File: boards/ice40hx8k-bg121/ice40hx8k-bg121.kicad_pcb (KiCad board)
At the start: 4 copper layers, 22.9 x 50.5 mm, 59 parts, among them J1 BANK 0, J2 BANK 1, J4 BANK 2, J5 BANK 3, U1 AP7361C_TO252_DPAK, U2 AP7361C_TO252_DPAK, U3 iCE40HX8K-BG121(121-Ball_caBG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, U4 ASDMB-xxxMHz

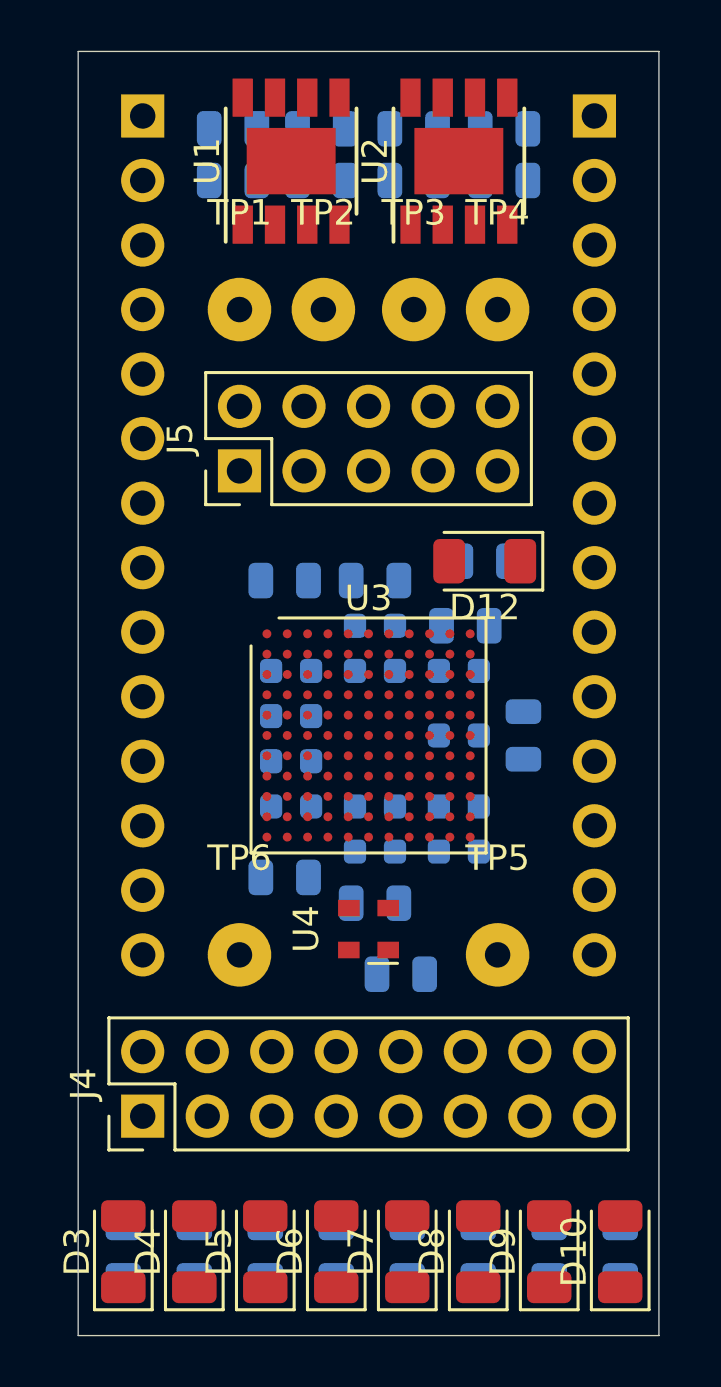
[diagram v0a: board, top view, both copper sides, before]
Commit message: Started putting down traces.
Still need to do C and differential pairs D.
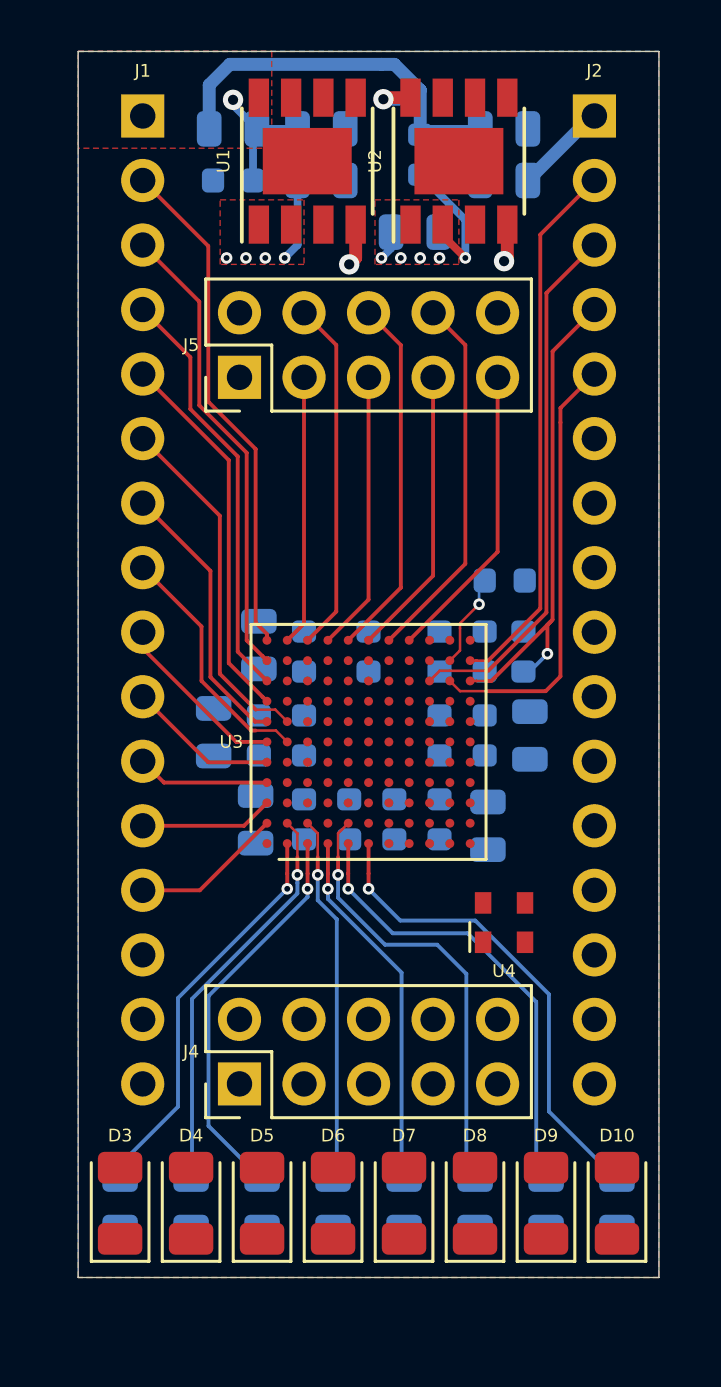
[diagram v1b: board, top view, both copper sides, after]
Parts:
- removed D12: CDONE, LED_SMD:LED_1206_3216Metric
- removed R15: 4k7, Diode_SMD:D_0805_2012Metric
- removed TP1: 3V3_EN, Connector_Wire:SolderWirePad_1x01_Drill1mm
- removed TP2: 1V2_IN, Connector_Wire:SolderWirePad_1x01_Drill1mm
- removed TP3: 1V2_OUT, Connector_Wire:SolderWirePad_1x01_Drill1mm
- removed TP4: 1V2_EN, Connector_Wire:SolderWirePad_1x01_Drill1mm
- removed TP5: OSC_STBY, Connector_Wire:SolderWirePad_1x01_Drill1mm
- removed TP6: FPGA_CLK, Connector_Wire:SolderWirePad_1x01_Drill1mm
- J1, J2: footprint Connector_PinHeader_2.54mm:PinHeader_1x14_P2.54mm_Vertical -> Connector_PinHeader_2.54mm:PinHeader_1x16_P2.54mm_Vertical
- J4: footprint Connector_PinHeader_2.54mm:PinHeader_2x08_P2.54mm_Vertical -> Connector_PinHeader_2.54mm:PinHeader_2x05_P2.54mm_Vertical
- R1, R13, R2: footprint Diode_SMD:D_0805_2012Metric -> Resistor_SMD:R_0603_1608Metric
- R10, R11, R12, R3, R4, R5, R6, R7, R8, R9: footprint Diode_SMD:D_0805_2012Metric -> Resistor_SMD:R_0805_2012Metric
- R14: value 220R -> 4k7; footprint Diode_SMD:D_0805_2012Metric -> Resistor_SMD:R_0603_1608Metric
- U1, U2: value AP7361C_TO252_DPAK -> AP7361C_SO-8EP
- moved R12 9.47 mm to (27.3, 45.5), turned to 90 degrees
- moved C9 8.99 mm to (38.1, 42.2), turned to 270 degrees
- moved C14 8.72 mm to (25.7, 42.0), turned to 90 degrees
- moved R11 8.25 mm to (36.4, 45.7), turned to 90 degrees
- moved D11 8.16 mm to (27.4, 38.6), turned to 90 degrees
- moved C17 7.94 mm to (36.3, 38.9), turned to 270 degrees
- moved C15 6.29 mm to (27.4, 42.2), turned to 90 degrees
- moved C10 6.29 mm to (36.3, 42.2), turned to 270 degrees
- moved C5 6.14 mm to (29.2, 38.9), turned to 270 degrees
- moved C7 6.14 mm to (34.5, 38.9), turned to 270 degrees
- moved R13 6.14 mm to (37.1, 36.1), turned to 0 degrees
- moved C6 5.86 mm to (29.2, 45.5), turned to 90 degrees
- moved C8 5.86 mm to (34.5, 45.5), turned to 90 degrees
- moved U4 5.34 mm to (37.1, 49.5), turned to 0 degrees
- moved C12 4.85 mm to (31.8, 38.9), turned to 270 degrees
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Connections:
- J1 pad 12: VCCIO_A -> IO_A10
- J1 pad 13: +3V3 -> IO_A11
- J1 pad 14: GND -> VCCIO_A
- J2 pad 10: IO_B08 -> IO_C03
- J2 pad 11: IO_B09 -> IO_C02
- J2 pad 12: VCCIO_B -> IO_C01
- J2 pad 13: +3V3 -> IO_C00
- J2 pad 14: GND -> VCCIO_B
- J2 pad 2: IO_B00 -> PROG_SCK
- J2 pad 3: IO_B01 -> PROG_SDI
- J2 pad 4: IO_B02 -> PROG_CRESET_B
- J2 pad 5: IO_B03 -> PROG_SDO
- J2 pad 6: IO_B04 -> IO_C07
- J2 pad 7: IO_B05 -> IO_C06
- J2 pad 8: IO_B06 -> IO_C05
- J2 pad 9: IO_B07 -> IO_C04
- J4 pad 1: IO_C00 -> +3V3
- J4 pad 10: PROG_CRESET_B -> GND
- J4 pad 2: +3V3 -> VCCIO_D
- J4 pad 3: IO_C01 -> IO_D00+
- J4 pad 4: VCCIO_C -> IO_D03
- J4 pad 5: IO_C02 -> IO_D00-
- J4 pad 6: PROG_SDO -> IO_D02-
- J4 pad 7: IO_C03 -> IO_D01+
- J4 pad 8: PROG_SDI -> IO_D02+
- J4 pad 9: IO_C04 -> IO_D01-
- J5 pad 1: IO_D00+ -> VCCIO_B
- J5 pad 3: IO_D00- -> IO_B00
- J5 pad 4: VCCIO_D -> IO_B06
- J5 pad 5: IO_D01+ -> IO_B01
- J5 pad 6: IO_D01- -> IO_B05
- J5 pad 7: IO_D02+ -> IO_B02
- J5 pad 8: IO_D03 -> IO_B04
- J5 pad 9: IO_D02- -> IO_B03
- R10 pad 1: IO_C00 -> IO_L0
- R14 pad 1: /ICE40HX8K/CDONE -> VCCIO_C
- R14 pad 2: Net-(D12-Pad1) -> PROG_CRESET_B
- R3 pad 1: IO_C07 -> IO_L7
- R4 pad 1: IO_C06 -> IO_L6
- R5 pad 1: IO_C05 -> IO_L5
- R6 pad 1: IO_C04 -> IO_L4
- R7 pad 1: IO_C03 -> IO_L3
- R8 pad 1: IO_C02 -> IO_L2
- R9 pad 1: IO_C01 -> IO_L1
- U1 pad 9: (no net) -> GND
- U2 pad 9: (no net) -> GND
- U3 pad A1: IO_A02 -> Net-(U3-PadA1)
- U3 pad A10: IO_A09 -> IO_A01
- U3 pad A11: IO_A08 -> IO_A00
- U3 pad A2: IO_A04 -> IO_A11
- U3 pad A3: IO_A03 -> IO_A10
- U3 pad A4: Net-(U3-PadA4) -> IO_A09
- U3 pad A5: Net-(U3-PadA5) -> IO_A08
- U3 pad A6: Net-(U3-PadA6) -> IO_A07
- U3 pad A7: Net-(U3-PadA7) -> IO_A05
- U3 pad A8: Net-(U3-PadA8) -> IO_A03
- U3 pad A9: Net-(U3-PadA9) -> IO_A02
- U3 pad B1: IO_D00+ -> IO_L7
- U3 pad B11: IO_B02 -> IO_B00
- U3 pad B2: IO_D00- -> IO_L6
- U3 pad B3: IO_A05 -> Net-(U3-PadB3)
- U3 pad B4: IO_A06 -> Net-(U3-PadB4)
- U3 pad B6: IO_A00 -> IO_A06
- U3 pad B7: IO_A01 -> IO_A04
- U3 pad C1: IO_D02- -> IO_L5
- U3 pad C11: IO_B03 -> IO_B06
- U3 pad C2: IO_D02+ -> IO_L4
- U3 pad C3: IO_D01- -> Net-(U3-PadC3)
- U3 pad C4: IO_D01+ -> Net-(U3-PadC4)
- U3 pad D1: IO_D03- -> IO_L3
- U3 pad D10: IO_B04 -> Net-(U3-PadD10)
- U3 pad D11: IO_B05 -> IO_B01
- U3 pad D5: IO_A07 -> Net-(U3-PadD5)
- U3 pad D9: IO_B07 -> Net-(U3-PadD9)
- U3 pad E1: IO_D03+ -> IO_L1
- U3 pad E10: IO_B00 -> Net-(U3-PadE10)
- U3 pad E11: IO_B06 -> IO_B05
- U3 pad E2: Net-(U3-PadE2) -> IO_L2
- U3 pad F1: Net-(U3-PadF1) -> IO_L0
- U3 pad F11: IO_B01 -> IO_B02
- U3 pad F3: IO_D04 -> IO_D03
- U3 pad G1: Net-(U3-PadG1) -> IO_D00-
- U3 pad G11: Net-(U3-PadG11) -> IO_B04
- U3 pad G2: Net-(U3-PadG2) -> IO_D00+
- U3 pad H1: Net-(U3-PadH1) -> IO_D02+
- U3 pad H11: Net-(U3-PadH11) -> IO_B03
- U3 pad H2: Net-(U3-PadH2) -> IO_D02-
- U3 pad J1: Net-(U3-PadJ1) -> IO_D01+
- U3 pad J11: IO_B08 -> Net-(U3-PadJ11)
- U3 pad J3: IO_C02 -> Net-(U3-PadJ3)
- U3 pad J4: IO_C05 -> Net-(U3-PadJ4)
- U3 pad K1: Net-(U3-PadK1) -> IO_D01-
- U3 pad K11: IO_B09 -> Net-(U3-PadK11)
- U3 pad K3: IO_C04 -> IO_C03
- U3 pad K4: Net-(U3-PadK4) -> IO_C05
- U3 pad K5: Net-(U3-PadK5) -> IO_C06
- U3 pad K6: IO_C00 -> IO_C07
- U3 pad K8: /ICE40HX8K/CDONE -> Net-(U3-PadK8)
- U3 pad L1: IO_C01 -> IO_C00
- U3 pad L2: IO_C03 -> IO_C01
- U3 pad L3: IO_C06 -> IO_C02
- U3 pad L4: IO_C07 -> IO_C04
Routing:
- net PROG_SCK: track 0.00 -> 21.3 mm
- net PROG_SDI: track 0.00 -> 21.0 mm
- net IO_A00: track 0.00 -> 20.1 mm
- net Net-(C3-Pad1): track 0.00 -> 19.7 mm, vias 0 -> 1
- net PROG_CRESET_B: track 0.00 -> 19.7 mm, vias 0 -> 1
- net IO_L0: track 0.00 -> 19.0 mm, vias 0 -> 1
- net IO_A01: track 0.00 -> 18.4 mm
- net IO_L1: track 0.00 -> 18.2 mm, vias 0 -> 1
- net IO_L2: track 0.00 -> 17.6 mm, vias 0 -> 1
- net PROG_SDO: track 0.00 -> 17.2 mm
- net IO_A02: track 0.00 -> 16.6 mm
- net IO_L7: track 0.00 -> 15.9 mm, vias 0 -> 1
- net IO_L6: track 0.00 -> 15.9 mm, vias 0 -> 1
- net IO_L5: track 0.00 -> 15.7 mm, vias 0 -> 1
- net IO_A03: track 0.00 -> 14.9 mm
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- added copper zone on F.Cu, net +1V2
- added copper zone on F.Cu, net +3V3
- added copper zone on In1.Cu, net +3V3
- added copper zone on F.Cu, net +5V
- added copper zone on B.Cu, net GND
- added copper zone on F.Cu, net GND
- added copper zone on In2.Cu, net GND
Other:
- board size 22.9 x 50.5 mm -> 22.9 x 48.3 mm
- net class Default: clearance 0.2 -> 0.0889
- rule trace_clearance: 0.2 -> 0.0889
- rule trace_min: 0.2 -> 0.0889
- rule via_min_drill: 0.3 -> 0.2
- rule via_min_size: 0.4 -> 0.45

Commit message: Starting ISL83488 breakout
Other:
- board text added: "Oh yeah, this thing can be like 1.5-2x long."
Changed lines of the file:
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@@
   (general
     (thickness 1.6)
-    (drawings 5)
+    (drawings 6)
     (tracks 222)
     (zones 0)
@@
     (39 F.Mask user)
     (40 Dwgs.User user hide)
-    (41 Cmts.User user hide)
+    (41 Cmts.User user)
     (42 Eco1.User user hide)
     (43 Eco2.User user hide)
@@
   )
   (setup
-    (last_trace_width 0.508)
+    (last_trace_width 0.25)
     (user_trace_width 0.1016)
     (user_trace_width 0.1524)
@@
     )
   )
+  (gr_text "Oh yeah, this thing can be like 1.5-2x long." (at 73.7616 35.306) (layer Cmts.User)
+    (effects (font (size 1.5 1.5) (thickness 0.3)))
+  )
   (dimension 17.78 (width 0.15) (layer Cmts.User)
     (gr_text "0.7000 in" (at 31.75 14.194) (layer Cmts.User)
@@
   (segment (start 37.211 22.0555) (end 37.211 23.368) (width 0.508) (layer F.Cu) (net 1))
   (segment (start 37.211 23.368) (end 37.084 23.495) (width 0.508) (layer F.Cu) (net 1))
-  (via (at 32.3342 17.1196) (size 0.8) (drill 0.4) (layers F.Cu B.Cu) (net 6))
   (via (at 26.162 23.368) (size 0.4572) (drill 0.2286) (layers F.Cu B.Cu) (net 2))
   (via (at 27.686 23.368) (size 0.4572) (drill 0.2286) (layers F.Cu B.Cu) (net 2))
@@
   (segment (start 27.3535 18.288) (end 26.416 17.3505) (width 0.3048) (layer B.Cu) (net 3))
   (via (at 26.416 17.145) (size 0.8) (drill 0.4) (layers F.Cu B.Cu) (net 3))
+  (via (at 32.3342 17.1196) (size 0.8) (drill 0.4) (layers F.Cu B.Cu) (net 6))
   (segment (start 36.1465 20.32) (end 36.1465 18.288) (width 0.3048) (layer B.Cu) (net 6))
   (segment (start 34.0105 18.288) (end 33.782 18.5165) (width 0.3048) (layer B.Cu) (net 6))

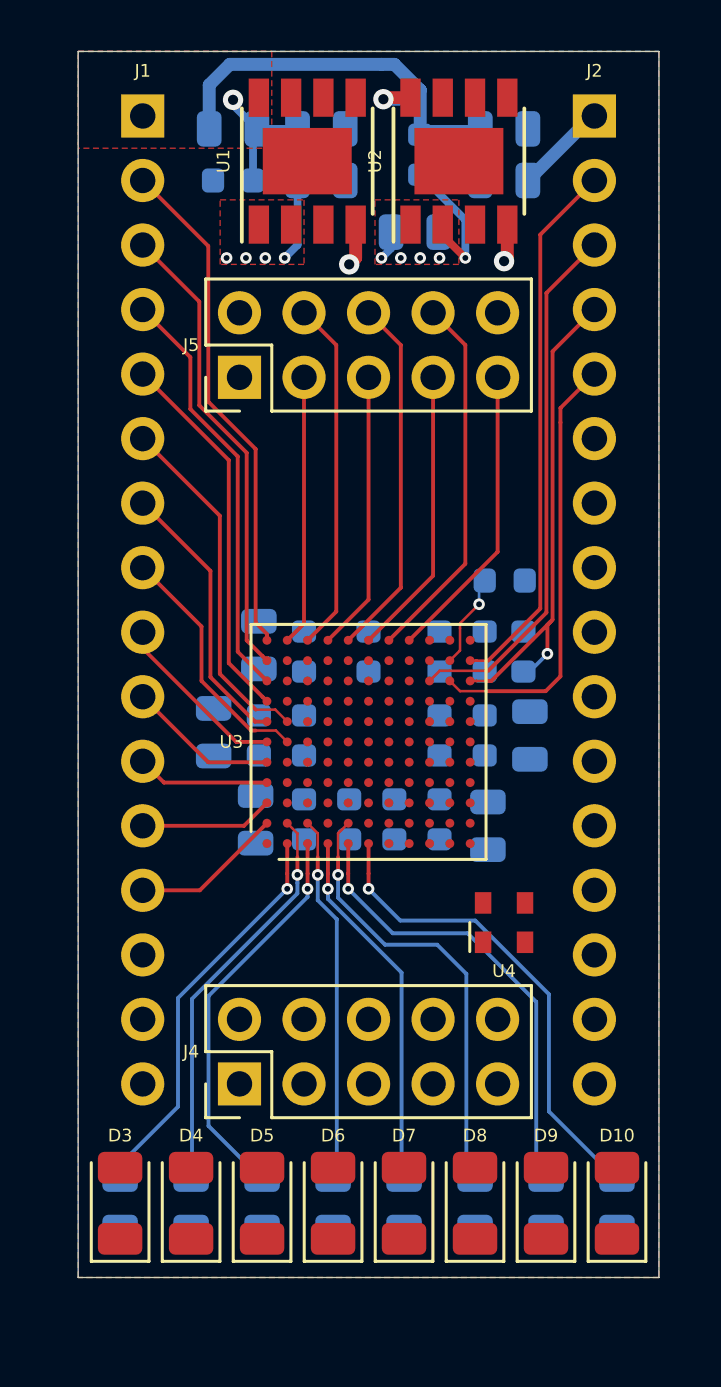
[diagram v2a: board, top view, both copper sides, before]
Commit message: No longer interested in ISL83488.
Layout for ICE40HX8K-BG121 -- just need power.
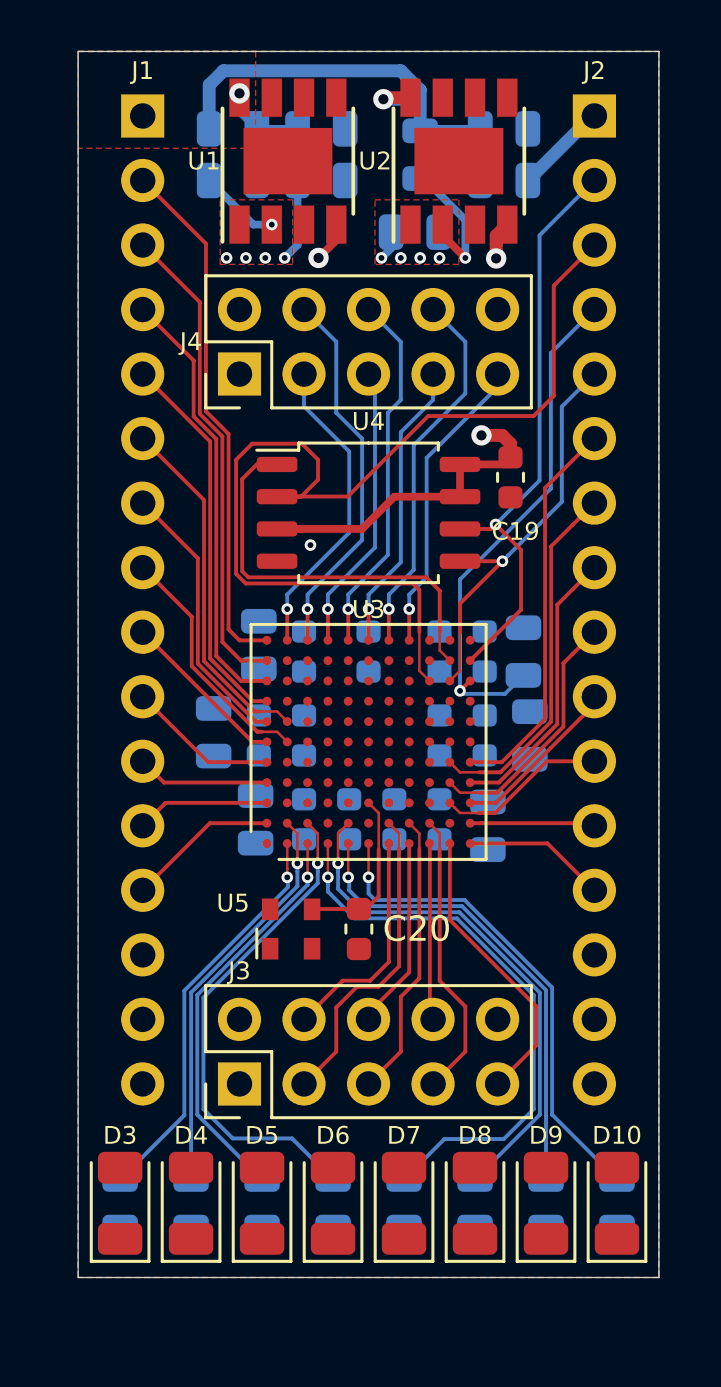
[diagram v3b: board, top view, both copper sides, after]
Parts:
- removed the R13 at (37.1, 36.1)
- added C19: 0.1u, Capacitor_SMD:C_0603_1608Metric, F.Cu at (37.3, 32.0)
- added C20: 22p, Capacitor_SMD:C_0603_1608Metric, F.Cu at (31.4, 49.8)
- added U5: ASDMB-xxxMHz, Oscillator:Oscillator_SMD_Abracon_ASDMB-4Pin_2.5x2.0mm, F.Cu at (28.7, 49.8)
- R1, R2: value 4k7 -> 10k; footprint Resistor_SMD:R_0603_1608Metric -> Resistor_SMD:R_0805_2012Metric
- R12: renamed from R14; value 4k7 -> 10k; footprint Resistor_SMD:R_0603_1608Metric -> Resistor_SMD:R_0805_2012Metric
- U4: value ASDMB-xxxMHz -> LE25U20AMB; footprint Oscillator:Oscillator_SMD_Abracon_ASDMB-4Pin_2.5x2.0mm -> Package_SO:SOIC-8_5.275x5.275mm_P1.27mm
- moved U4 17.0 mm to (31.8, 33.4)
- moved U1 0.76 mm to (28.6, 19.6)
- moved J4 0.13 mm to (26.7, 27.9)
- renumbered C18 to C17, C17 to C18, J4 to J3, J5 to J4, R12 to R13
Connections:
- net IO_D00+ renamed IO_D05
- net IO_D01- renamed IO_D00
- net Net-(U3-PadH9) renamed CBSEL1
- net Net-(U3-PadL8) renamed CBSEL0
- J2 pad 14: VCCIO_B -> VCCIO_C
- J3 pad 4: IO_D03 -> IO_D06
- J3 pad 5: IO_D00- -> IO_D03
- J3 pad 6: IO_D02- -> IO_D04
- J3 pad 7: IO_D01+ -> IO_D01
- J3 pad 8: IO_D02+ -> IO_D02
- U1 pad 9: GND -> (no net)
- U2 pad 9: GND -> (no net)
- U3 pad F3: IO_D03 -> /ICE40HX8K/FPGA_CLK
- U3 pad G1: IO_D00- -> IO_D06
- U3 pad H1: IO_D02+ -> IO_D04
- U3 pad H2: IO_D02- -> IO_D03
- U3 pad J1: IO_D01+ -> IO_D02
- U3 pad J2: Net-(U3-PadJ2) -> IO_D01
- U3 pad K10: PROG_SS -> PROG_SS_B
- U3 pad K3: IO_C03 -> IO_C02
- U3 pad K4: IO_C05 -> IO_C04
- U3 pad K6: IO_C07 -> Net-(U3-PadK6)
- U3 pad L3: IO_C02 -> IO_C03
- U3 pad L4: IO_C04 -> IO_C05
- U3 pad L5: /ICE40HX8K/FPGA_CLK -> IO_C07
- U4 pad 1: Net-(U4-Pad1) -> PROG_SS_B
- U4 pad 2: GND -> PROG_SDI
- U4 pad 3: /ICE40HX8K/FPGA_CLK -> VCCIO_C
- U4 pad 4: +3V3 -> GND
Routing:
- net PROG_SDI: track 21.0 -> 41.3 mm
- net PROG_SS_B: track 0.00 -> 16.2 mm
- net IO_C07: track 0.00 -> 15.5 mm
- net IO_C06: track 0.00 -> 14.3 mm
- net VCCIO_C: track 0.00 -> 12.9 mm, vias 0 -> 1
- net IO_D05: track 0.00 -> 12.5 mm
- net IO_D00: track 0.00 -> 11.5 mm
- net IO_D01: track 0.00 -> 11.4 mm
- net IO_D03: track 0.00 -> 11.3 mm
- net IO_C05: track 0.00 -> 11.1 mm
- net IO_C04: track 0.00 -> 10.5 mm
- net IO_D06: track 0.00 -> 8.94 mm
- net IO_L3: track 14.5 -> 22.4 mm
- net IO_D04: track 0.00 -> 7.58 mm
- net IO_C02: track 0.00 -> 7.41 mm
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
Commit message: Fanout of BGA, and power.
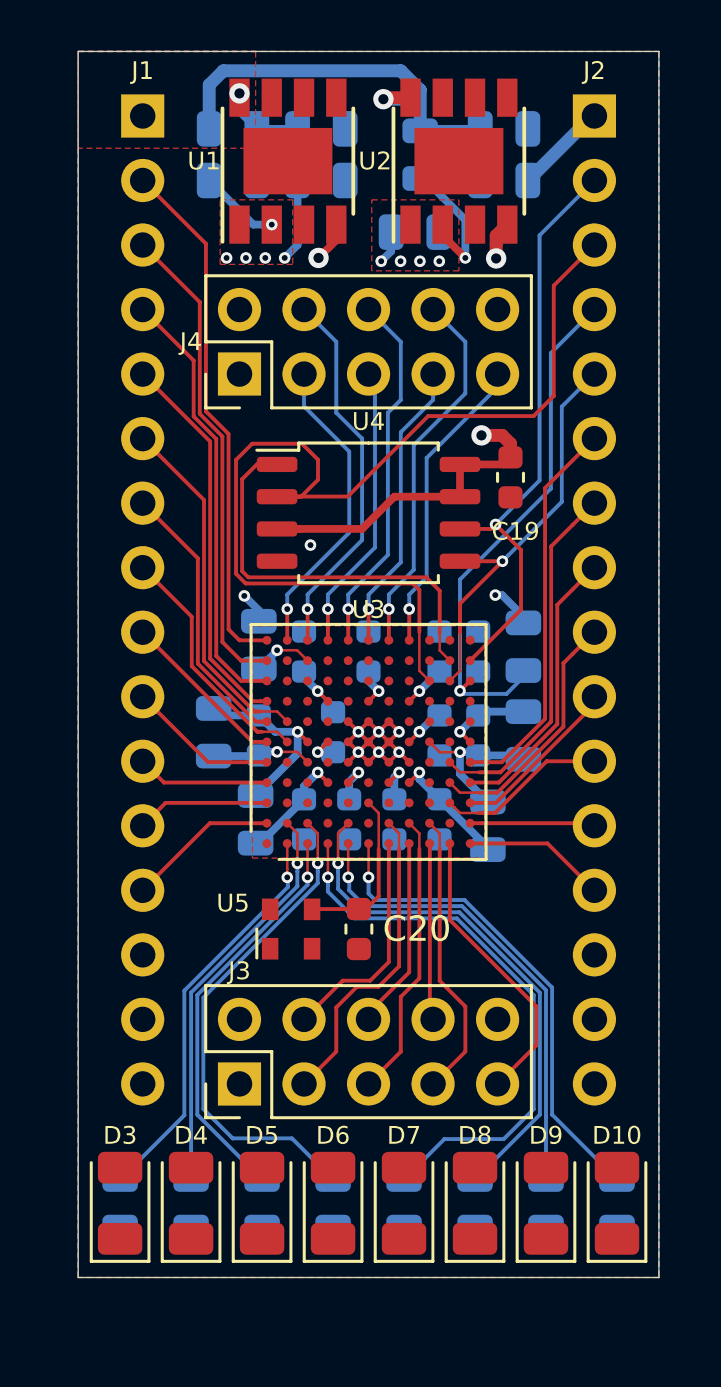
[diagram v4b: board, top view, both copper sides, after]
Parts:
- moved C11 1.15 mm to (30.4, 42.0)
- moved C10 0.25 mm to (36.1, 42.2)
- moved C18 0.25 mm to (36.1, 38.9)
- moved C9 0.25 mm to (37.8, 42.2)
- moved R12 0.19 mm to (37.8, 38.7)
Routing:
- net VCCIO_C: track 12.9 -> 43.2 mm, vias 1 -> 3
- net VCCIO_D: track 0.00 -> 19.9 mm, vias 0 -> 2
- net VCCIO_B: track 0.00 -> 19.2 mm, vias 0 -> 1
- net +1V2: track 1.17 -> 14.4 mm, vias 4 -> 8
- net VCCIO_A: track 0.00 -> 12.3 mm, vias 0 -> 1
- net GND: track 3.12 -> 15.0 mm, vias 3 -> 9
- net /ICE40HX8K/VCCPLL1: track 0.00 -> 7.44 mm, vias 0 -> 1
- net /ICE40HX8K/VCCPLL0: track 0.00 -> 6.65 mm, vias 0 -> 1
- net /ICE40HX8K/GNDPLL1: track 0.00 -> 3.93 mm, vias 0 -> 1
- net /ICE40HX8K/GNDPLL0: track 0.00 -> 3.64 mm, vias 0 -> 1
- net Net-(D11-Pad1): track 0.00 -> 2.40 mm, vias 0 -> 1
- net +3V3: track 6.93 -> 8.17 mm, vias 4 -> 5
- added copper zone on In1.Cu, net +1V2
